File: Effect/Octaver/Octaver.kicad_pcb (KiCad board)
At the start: 2 copper layers, 30 x 57 mm, 25 parts, among them J1 Conn_01x04_Pin, Q1 DMMT5551, Q2 DMMT5551

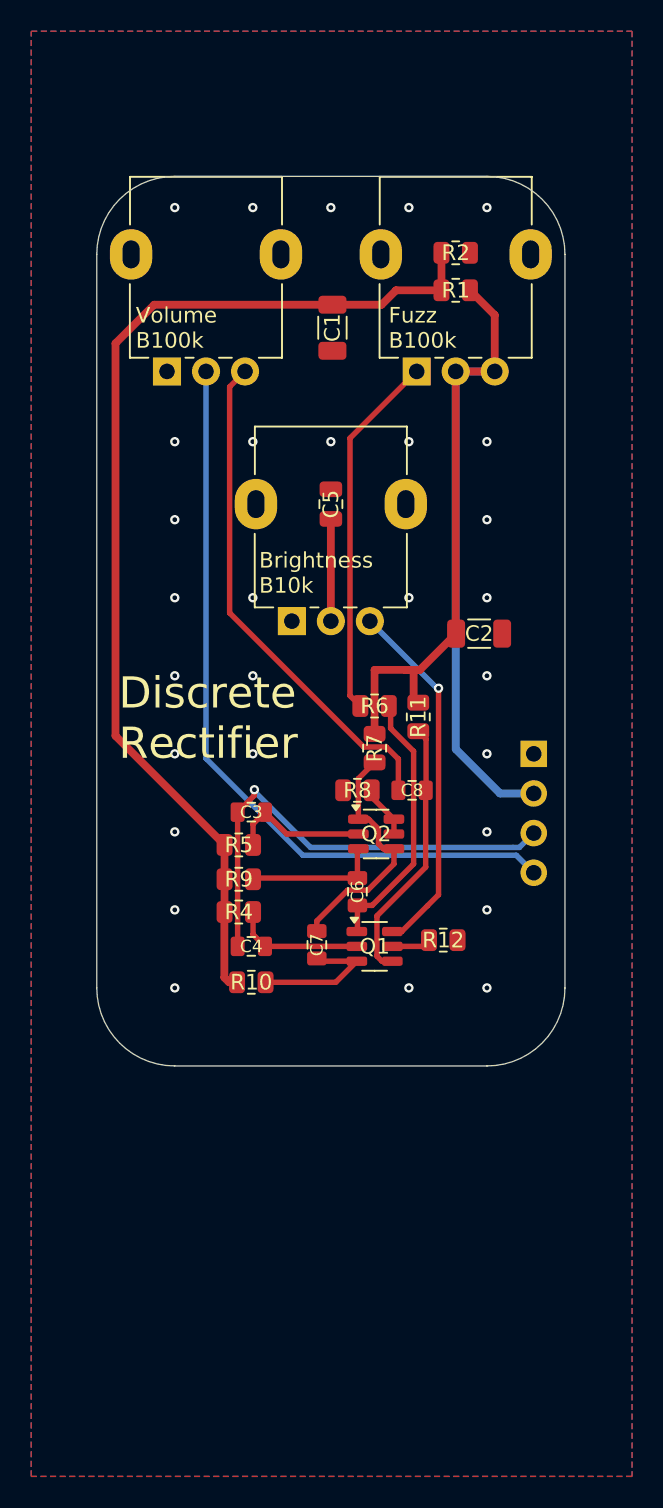
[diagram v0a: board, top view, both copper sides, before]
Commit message: First revisions from gen3 testing...
It turns out that while the single connector was sufficient, it is also
mechanically annoyingly less robust than the two separate pin headers we
used to have.

So even though we don't need the extra pins, just split it up into
"power" and a "signal" connectors again.  The placement behind the
output jack was good, so just put the power jack behind the input one
instead.

That ends up making routing nicer with the power trace going down where
it needs to be for the LED anyway, so it's a win-win.  Much nicer than
the old board.  And with the extra pins and the position right next to
the LED, lets just make the base board LED voltage available as an
"active" signal in case anybody ever wants it.

Also, just move the DC blocking capacitor and the anti-pop resistor to
ground to the base board.  Any effects board needs to do that, so it's
one less thing to worry about.  Also add back the low pass RF filter.

With the connector change, this obviously makes the new boards
incompatible, but it's not like I have any legacy boards except for the
test-boards.

On the effect board side, this does the layout changes, but also fixes
the Octaver board that was half-arsed and hadn't done proper bias
voltage calculations.  This basically just reuses them from the boost
board.

Plus use a JFET input on for the Octaver, and while at it make it also
just split the phase the natural way.  Both simpler and more balanced.

So maybe the Octaver works now.

And by "works", I obviously don't mean "sounds good".

Signed-off-by: Linus Torvalds <torvalds@linux-foundation.org>
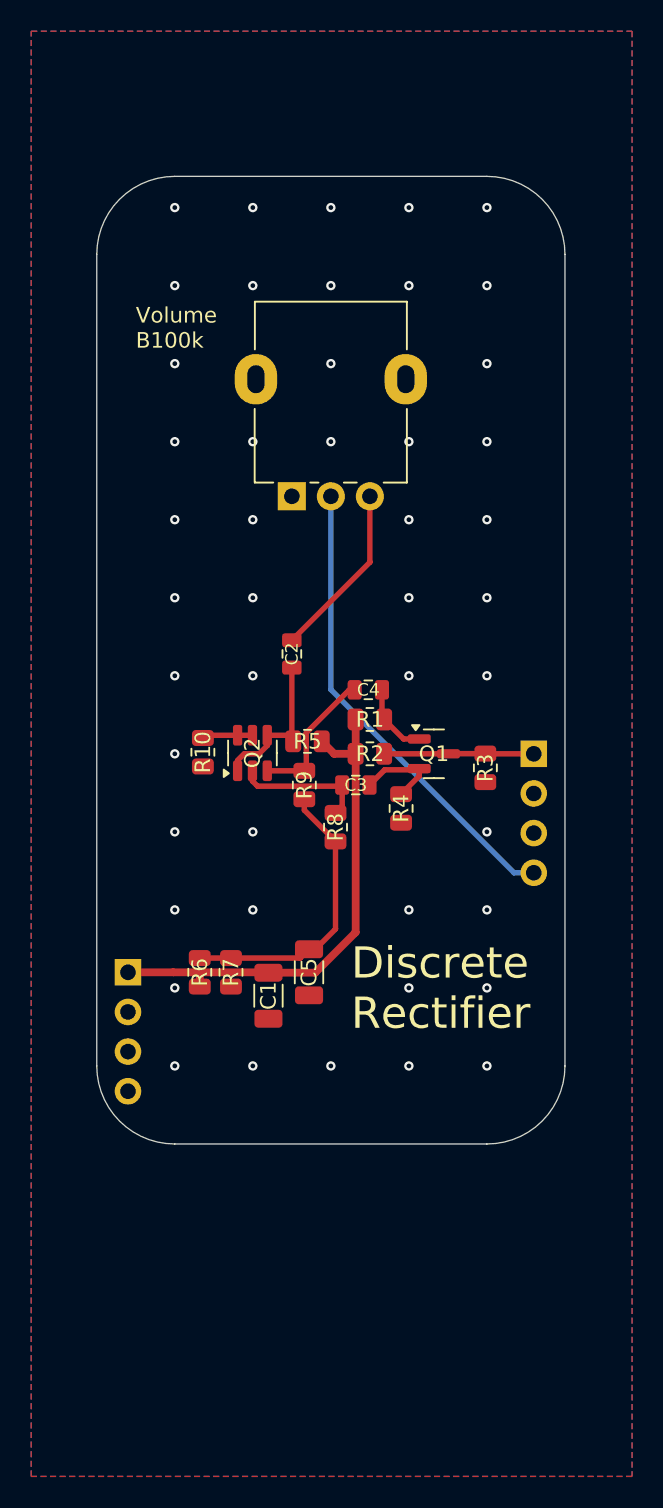
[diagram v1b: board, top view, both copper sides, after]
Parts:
- removed the C4 at (94.9, 112.3)
- removed the C5 at (100.0, 84.0)
- removed C7, C8: 0.1uF, Mylib:C_0704_1810Metric
- removed the R10 at (94.9, 114.6)
- removed R11: 10k, Resistor_SMD:R_0805_2012Metric
- removed R12: 2.2k, Resistor_SMD:R_0805_2012Metric
- removed the R6 at (102.8, 96.9)
- removed the RV1 at (108.0, 68.0)
- removed RV2: 10k, Mylib:Potentiometer_9mm_MP
- added C2: 0.1uF, Mylib:C_0704_1810Metric, F.Cu at (97.5, 93.6)
- added J2: Conn_01x04_Pin, Connector_PinHeader_2.54mm:PinHeader_1x04_P2.54mm_Vertical, B.Cu at (87.0, 114.0)
- added R1: 3k3, Resistor_SMD:R_0805_2012Metric, F.Cu at (102.5, 97.8)
- added R2: 2MEG, Resistor_SMD:R_0805_2012Metric, F.Cu at (102.5, 100.0)
- added R3: 1MEG, Resistor_SMD:R_0805_2012Metric, F.Cu at (109.9, 100.9)
- Q1: value DMMT5551 -> MMBFJ201; footprint Package_TO_SOT_SMD:SOT-23-6 -> Package_TO_SOT_SMD:SOT-23
- R10: renamed from R8; value 10k -> 3k3
- R4: value 470k -> 3k3
- R6: renamed from R1; value 10k -> 100k
- R7: renamed from R2; value 10k -> 33k
- R8: renamed from R5; value 470k -> 100k
- R9: value 470k -> 100k
- moved R7 48.3 mm to (93.6, 114.0), turned to -90 degrees
- moved R6 46.7 mm to (91.6, 114.0), turned to 90 degrees
- moved C5 41.3 mm to (98.6, 114.0)
- moved C1 26.8 mm to (96.0, 115.5), turned to -90 degrees
- moved C4 13.0 mm to (102.4, 95.9), turned to 0 degrees
- moved Q1 12.9 mm to (106.6, 100.0)
- moved R4 12.3 mm to (104.5, 103.5), turned to -90 degrees
- moved RV1 11.3 mm to (100.0, 76.0)
- moved R10 10.2 mm to (91.8, 99.9), turned to -90 degrees
- moved Q2 9.47 mm to (95.0, 99.9), turned to 90 degrees
- moved R9 7.35 mm to (98.3, 102.0), turned to 90 degrees
- moved C3 6.92 mm to (101.6, 102.0), turned to 180 degrees
- moved R8 6.30 mm to (100.3, 104.7), turned to 90 degrees
- moved R5 4.32 mm to (98.5, 99.2), turned to 180 degrees
- renumbered C2 to C1, C6 to C4, C1 to C5, R7 to R5, RV3 to RV1
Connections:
- net NOT_IN renamed NOT_BUF
- C3 pad 1: IN -> BUF
- J1 pad 1: GND -> IN
- J1 pad 2: +V -> GND
- J1 pad 3: IN -> GND
- Q1 pad 2: Net-(Q1A-B) -> BUF
- Q1 pad 3: Net-(Q1B-B) -> IN
- R4 pad 1: VBIAS -> BUF
- R4 pad 2: Net-(Q1A-B) -> GND
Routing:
- net VBIAS: track 69.2 -> 18.2 mm
- net +V: track 71.1 -> 32.7 mm
- net Net-(R6-Pad1): track 23.5 -> 0.00 mm
- net Net-(Q1A-E): track 23.3 -> 0.00 mm, vias 1 -> 0
- net Net-(C2-Pad2): track 32.6 -> 11.3 mm
- net IN: track 30.4 -> 9.62 mm, vias 1 -> 0
- net OUT: track 48.8 -> 30.2 mm
- net Net-(Q1B-C): track 17.0 -> 0.00 mm
- net NOT_BUF: track 17.2 -> 4.72 mm
- net Net-(Q1B-B): track 9.04 -> 0.00 mm
- net Net-(Q1A-B): track 8.40 -> 0.00 mm
- net Net-(C5-Pad2): track 6.55 -> 0.00 mm
- net BUF: track 0.00 -> 5.74 mm
- net RECT: track 15.8 -> 10.2 mm
- net Net-(Q1B-E): track 2.52 -> 0.00 mm
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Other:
- board size 30 x 57 mm -> 30 x 62 mm
- board text removed: "Brightness B10k"
- board text removed: "Fuzz B100k"

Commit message: More octaver circuit impedance tweaking
I decided that the JFET phase splitter is the right way to go after all,
and that I just need to make sure the output impedance is low enough for
the following circuit.  Smaller transistors, more current, stiffer
signals.

But "more current" in this case is still in the "a couple of mA" range,
and this isn't battery-operated, so to quote Alfred E Neuman: "What, me
worry?"

I'm not particularly happy with that output side, and I'll probably
continue to play with this to get a better feel for the whole input and
output impedance of the different transistor circuits.  But maybe it's
time to make another test pcb just to see if this works in reality at
all.

Signed-off-by: Linus Torvalds <torvalds@linux-foundation.org>
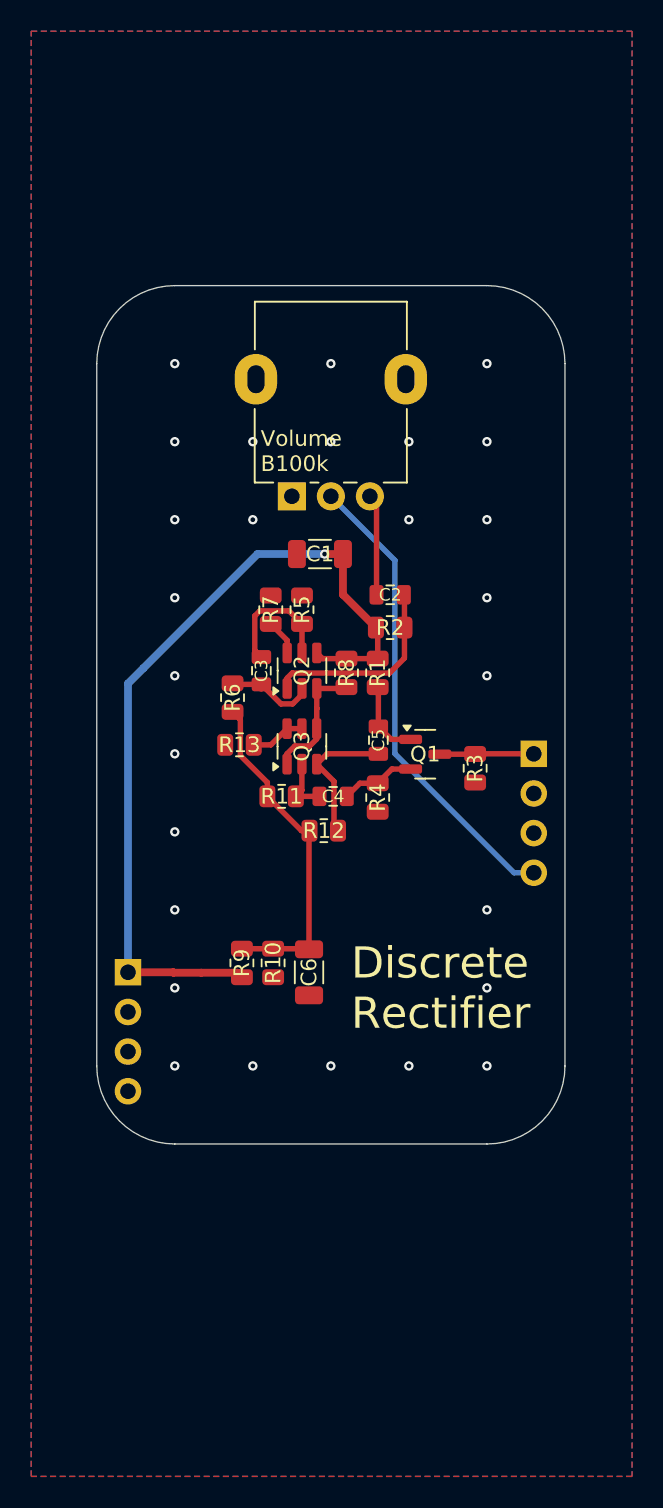
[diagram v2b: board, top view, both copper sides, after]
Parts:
- added C3: 0.1uF, Mylib:C_0704_1810Metric, F.Cu at (95.5, 94.7)
- added Q2: DMMT5551, Package_TO_SOT_SMD:SOT-23-6, F.Cu at (98.2, 94.7)
- added R5: 33k, Resistor_SMD:R_0805_2012Metric, F.Cu at (98.2, 90.8)
- added R6: 470k, Resistor_SMD:R_0805_2012Metric, F.Cu at (93.7, 96.4)
- added R7: 3k3, Resistor_SMD:R_0805_2012Metric, F.Cu at (96.2, 90.8)
- Q1: value MMBFJ201 -> MMBF5103
- R1, R4: value 3k3 -> 1k
- R10: renamed from R7; value 33k -> 47k
- R11: renamed from R8; value 100k -> 470k
- R12: renamed from R9; value 100k -> 470k
- R13: renamed from R10; value 3k3 -> 10k
- R2: value 2MEG -> 10k
- R8: renamed from R5; value 10k -> 22k
- moved C1 28.5 mm to (99.3, 87.2), turned to 180 degrees
- moved R2 8.19 mm to (103.8, 91.9)
- moved C2 7.35 mm to (103.8, 89.8), turned to 180 degrees
- moved R8 5.05 mm to (101.0, 94.8), turned to -90 degrees
- moved R11 3.98 mm to (96.8, 102.7), turned to 0 degrees
- moved C5 3.29 mm to (103.0, 99.1), turned to 90 degrees
- moved Q3 3.20 mm to (98.1, 99.5)
- moved R12 3.18 mm to (99.5, 104.9), turned to 0 degrees
- moved R1 3.03 mm to (103.0, 94.8), turned to -90 degrees
- moved R10 2.77 mm to (96.3, 113.4)
- moved R9 2.77 mm to (94.3, 113.4)
- moved R13 2.39 mm to (94.1, 99.4), turned to 180 degrees
- moved R4 1.66 mm to (103.0, 102.8)
- moved C4 1.63 mm to (100.1, 102.7)
- moved R3 0.66 mm to (109.2, 100.9)
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- renumbered C3 to C4, C4 to C5, C5 to C6, Q2 to Q3, R6 to R9
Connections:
- net NOT_BUF renamed BUF_NOT
- C2 pad 1: RECT -> Net-(Q2A-C)
- R2 pad 2: IN -> Net-(Q2A-C)
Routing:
- net +V: track 32.7 -> 54.8 mm, vias 0 -> 1
- net Net-(Q2A-C): track 0.00 -> 12.8 mm
- net Net-(Q2B-E): track 0.00 -> 8.81 mm
- net Net-(Q2A-B): track 0.00 -> 5.93 mm
- net Net-(C2-Pad2): track 11.3 -> 6.49 mm
- net Net-(Q3A-B): track 8.54 -> 3.74 mm
- net IN: track 9.62 -> 6.03 mm
- net VBIAS: track 18.2 -> 21.5 mm
- net Net-(Q2A-E): track 0.00 -> 2.29 mm
- net RECT: track 10.2 -> 8.13 mm
- net BUF: track 5.74 -> 4.81 mm
- net GND: vias 46 -> 27
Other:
- board size 30 x 62 mm -> 30 x 55 mm

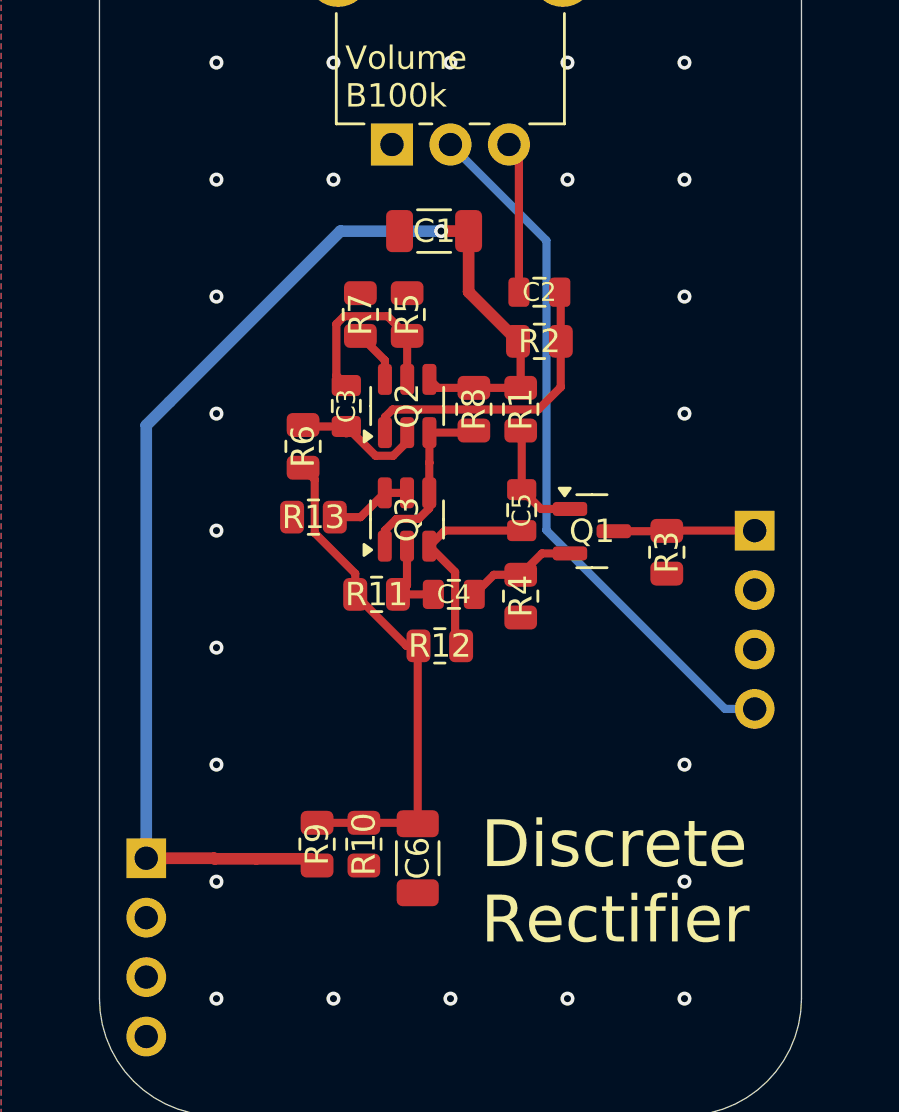
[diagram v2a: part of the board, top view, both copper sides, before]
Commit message: Update Octaver for bass frequencies
This is just updating the 0.1uF caps to 1uF, which gives much better
low-frequency behavior.  That does mean replacing the small 0704 form
factor with a 1206 one, so the pcb layout changes a bit.

It also means not using C0G caps, but let's be honest here: audiophile
this is not.

Signed-off-by: Linus Torvalds <torvalds@linux-foundation.org>
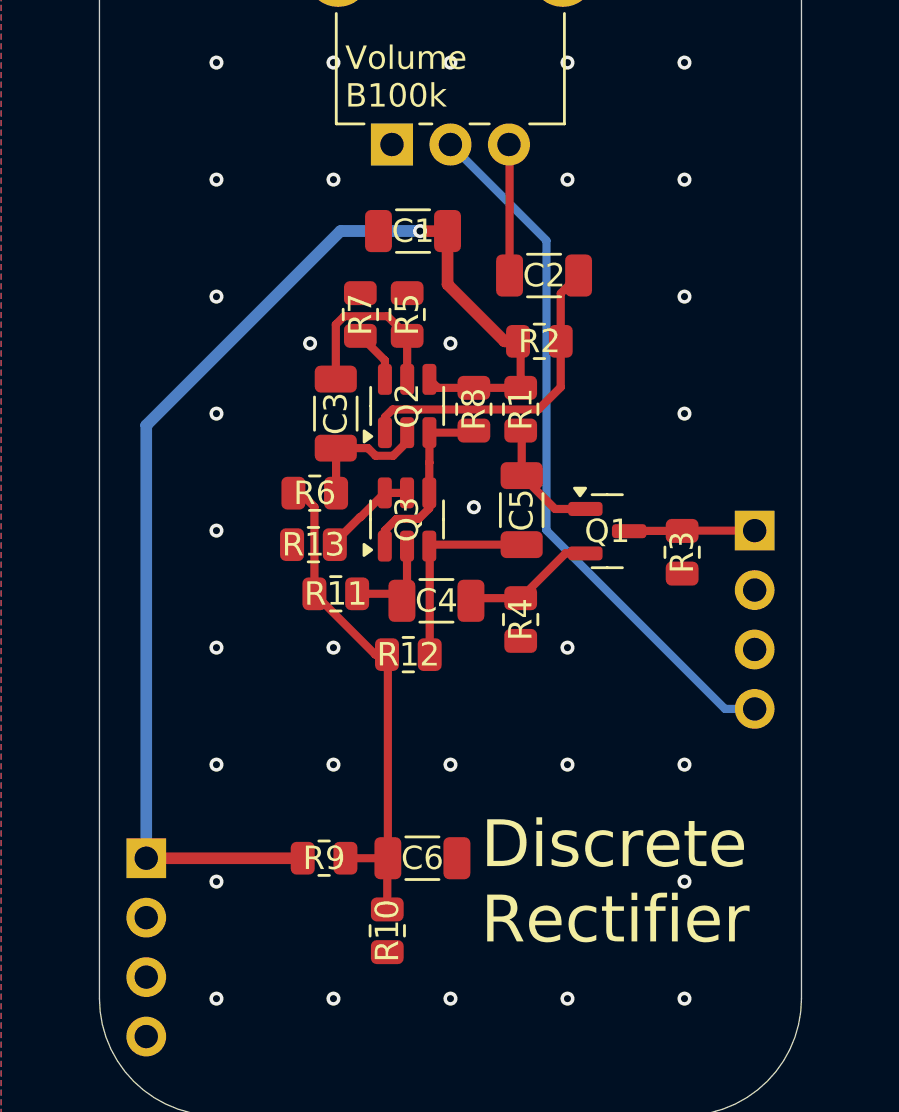
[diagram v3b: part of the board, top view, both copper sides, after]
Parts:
- C2, C3, C4, C5: value 0.1uF -> 1uF; footprint Mylib:C_0704_1810Metric -> Capacitor_SMD:C_1206_3216Metric
- moved R10 3.83 mm to (97.3, 117.1)
- moved R6 2.06 mm to (94.2, 98.4), turned to 0 degrees
- moved R11 1.74 mm to (95.1, 102.7)
- moved R12 1.40 mm to (98.2, 105.3)
- moved R13 1.17 mm to (94.1, 100.6)
- moved R4 1.00 mm to (103.0, 103.8)
- moved C1 0.90 mm to (98.4, 87.2)
- moved C4 0.79 mm to (99.4, 103.0)
- moved C2 0.74 mm to (104.0, 89.1)
- moved R9 0.67 mm to (94.6, 114.0), turned to 0 degrees
- moved Q1 0.66 mm to (106.7, 100.0)
- moved R3 0.66 mm to (109.9, 100.9)
- moved C3 0.56 mm to (95.1, 95.0)
- moved C6 0.20 mm to (98.8, 114.0), turned to 0 degrees
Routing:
- net Net-(Q2A-C): track 12.8 -> 13.8 mm
- net +V: track 54.8 -> 53.9 mm
- net BUF: track 4.81 -> 5.73 mm
- net Net-(C2-Pad2): track 6.49 -> 5.61 mm
- net Net-(Q3A-B): track 3.74 -> 4.46 mm
- net IN: track 6.03 -> 5.37 mm
- net Net-(Q3A-E): track 3.52 -> 4.06 mm
- net GND: vias 27 -> 35
